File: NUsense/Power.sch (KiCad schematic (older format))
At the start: 36 parts, among them Q1201 BC807, Q1202 2N3055, Q1203 Q_NMOS_GDS, Q1204 Q_NMOS_GDS, Q1205 2N2219, Q1206 Q_PMOS_GDS, SW1201 SW_SPDT, U1201 LD1086D2M33

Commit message: Cleans up some minor things
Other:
- note added: "For limiting inrush current"
- note added: "To current sensor"
- note removed: "Limit inrush current"
- moved on the sheet: C1201, C1202, C1203, C1204, C1205, C1206, C1207, C1208, C1209, C1210, C1211, D1201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

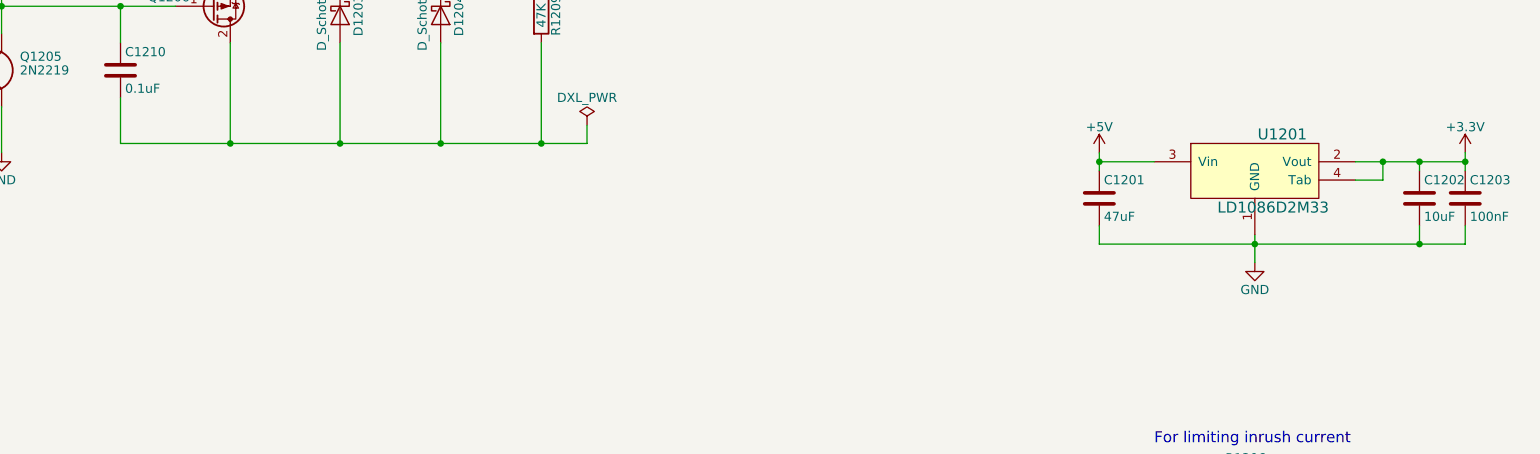
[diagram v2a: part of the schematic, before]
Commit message: Add labels
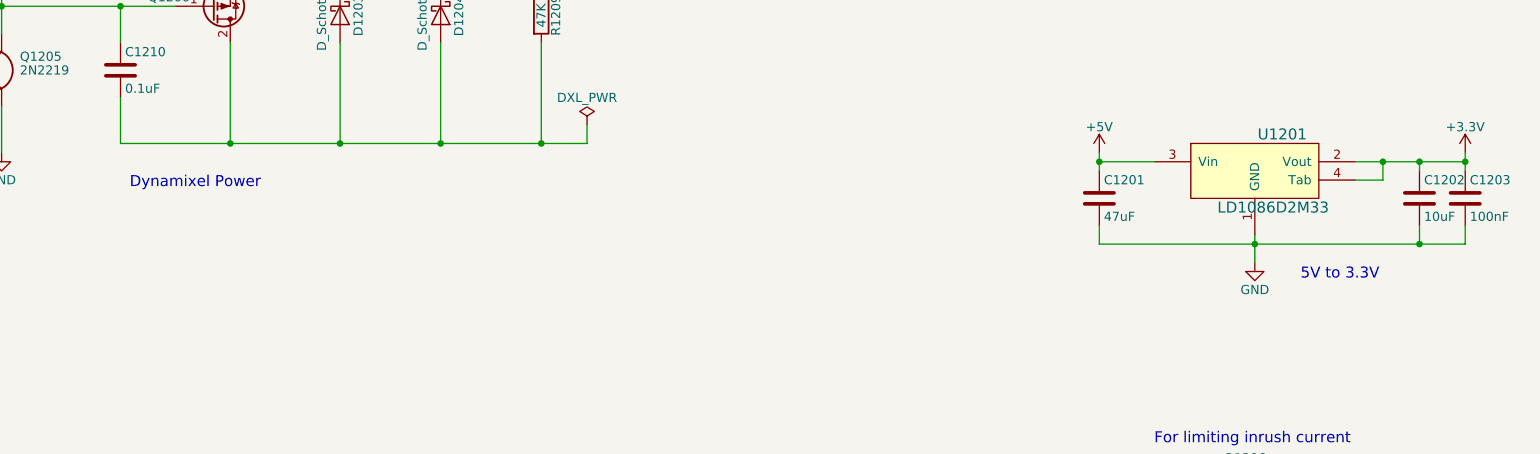
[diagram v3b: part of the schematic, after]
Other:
- note added: "5V to 3.3V"
- note added: "Dynamixel Power"
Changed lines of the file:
@@
 	6600 4600 6600 4500
 Connection ~ 6350 4600
+Text Notes 4100 4850 0    60   ~ 0
+Dynamixel Power
+Text Notes 10500 5350 0    60   ~ 0
+5V to 3.3V
 $EndSCHEMATC
